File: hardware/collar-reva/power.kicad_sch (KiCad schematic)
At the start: 12 parts, among them J1 USB-C, J2 JST-PH LiPo, U2 MCP73831, U3 AP2112K-3.3

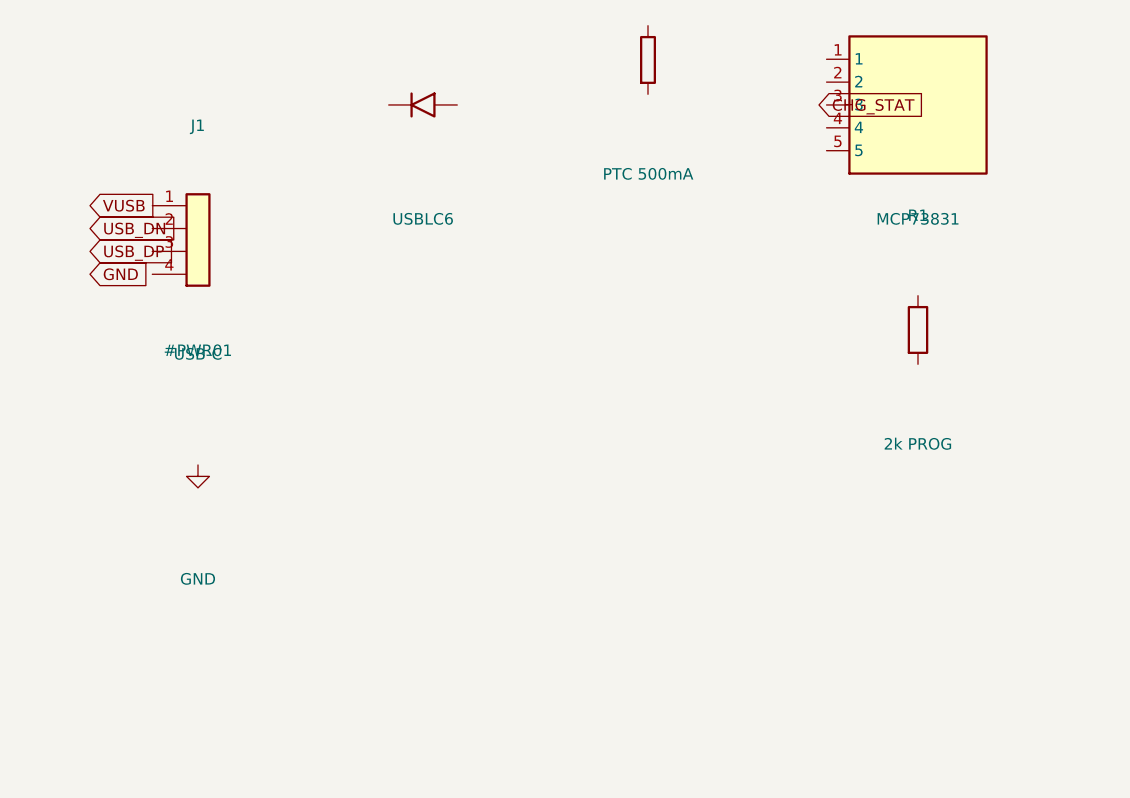
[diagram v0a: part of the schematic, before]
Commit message: feat(collar): ESP32-S3 firmware and neck PPG (#34)
* feat(collar): ESP32-S3 firmware and TI AFE4404 neck PPG

Host-tested HR/HRV, IMU RMS, and 1 Hz frames plus Arduino bring-up. Schematic adds the ventral-neck optical AFE on I2C so the puck can read pulse without actuation.

Co-authored-by: Cursor <cursoragent@cursor.com>

* feat(firmware): wire IMU, VBAT, and audio features into the collar loop

Bring-up now reads BMI270 accel and AFE4404 IR, converts VBAT on the derived divider, and keeps BLE notify-only.

Co-authored-by: Cursor <cursoragent@cursor.com>

* feat(firmware): I2S mic hop and VBAT-empty fault priority

INMP441 now feeds audio RMS/bark on the Rev-A pin map, and a low cell overrides a missing PPG peak so the 1 Hz frame reports the more urgent fault.

Co-authored-by: Cursor <cursoragent@cursor.com>

* feat(firmware): emit Phase-2 CBOR frames and check BMI270 chip ID

The 1 Hz notify is a real CBOR map (not JSON), and bring-up NAKs a missing IMU so we do not silently stream zeros.

Co-authored-by: Cursor <cursoragent@cursor.com>

* docs(firmware): note I2S RX pins in the collar bring-up order

Co-authored-by: Cursor <cursoragent@cursor.com>

* feat(firmware): pack 1 Hz CBOR to a BLE notify MTU

Frames now clip to MTU-3 so a default 23-byte ATT MTU cannot silently truncate the Phase-2 map once NimBLE is attached.

Co-authored-by: Cursor <cursoragent@cursor.com>

* feat(firmware): NimBLE advertise aarf-collar and notify 1 Hz CBOR

Phone can subscribe to the notify-only GATT char. LED and WDT follow the fault table, and IMU/mic NAKs now beat a missing PPG peak.

Co-authored-by: Cursor <cursoragent@cursor.com>

* feat(firmware): BMI270 accel bring-up and NVS VBAT cal

Soft-reset and enable ±8 g accel after chip-ID, and load divider scale/offset from NVS so bench cal survives reboot. PlatformIO build stays green.

Co-authored-by: Cursor <cursoragent@cursor.com>

* feat(firmware): bark CLIP to /infer/audio plus AFE4404 4 mA init

Wi-Fi posts the existing runtime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
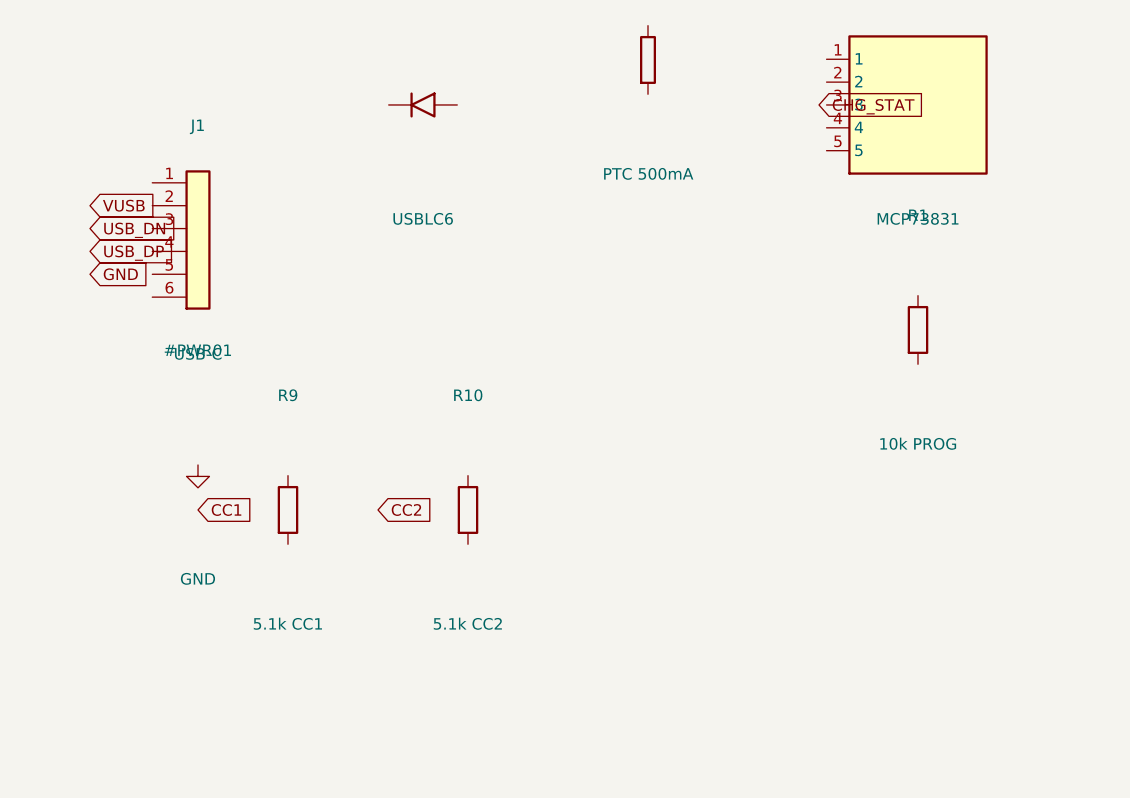
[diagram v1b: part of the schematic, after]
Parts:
- removed J1: USB-C, symbol Connector:Conn_01x04
- added J1: USB-C, Connector_USB:USB_C_Receptacle_USB4105-xx-A_16P_TopMnt_Horizontal, symbol Connector:Conn_01x06
- added R10: 5.1k CC2, Resistor_SMD:R_0402_1005Metric, symbol Device:R
- added R9: 5.1k CC1, Resistor_SMD:R_0402_1005Metric, symbol Device:R
- C1, C2: footprint (none) -> Capacitor_SMD:C_0805_2012Metric
- C3: footprint (none) -> Capacitor_SMD:C_0402_1005Metric
- D1: footprint (none) -> Package_TO_SOT_SMD:SOT-23-6
- F1: footprint (none) -> Fuse:Fuse_1812_4532Metric
- J2: footprint (none) -> Connector_JST:JST_PH_S2B-PH-SM4-TB_1x02-1MP_P2.00mm_Horizontal
- R1: value 2k PROG -> 10k PROG; footprint (none) -> Resistor_SMD:R_0402_1005Metric
- R2, R3: footprint (none) -> Resistor_SMD:R_0402_1005Metric
- U2, U3: footprint (none) -> Package_TO_SOT_SMD:SOT-23-5
